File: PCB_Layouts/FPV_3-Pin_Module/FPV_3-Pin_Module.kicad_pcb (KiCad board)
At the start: 2 copper layers, 33.5 x 25.2 mm, 4 parts, among them J1 Conn_01x03_Socket, J2 Conn_01x10_Socket, J3 Conn_01x10_Socket

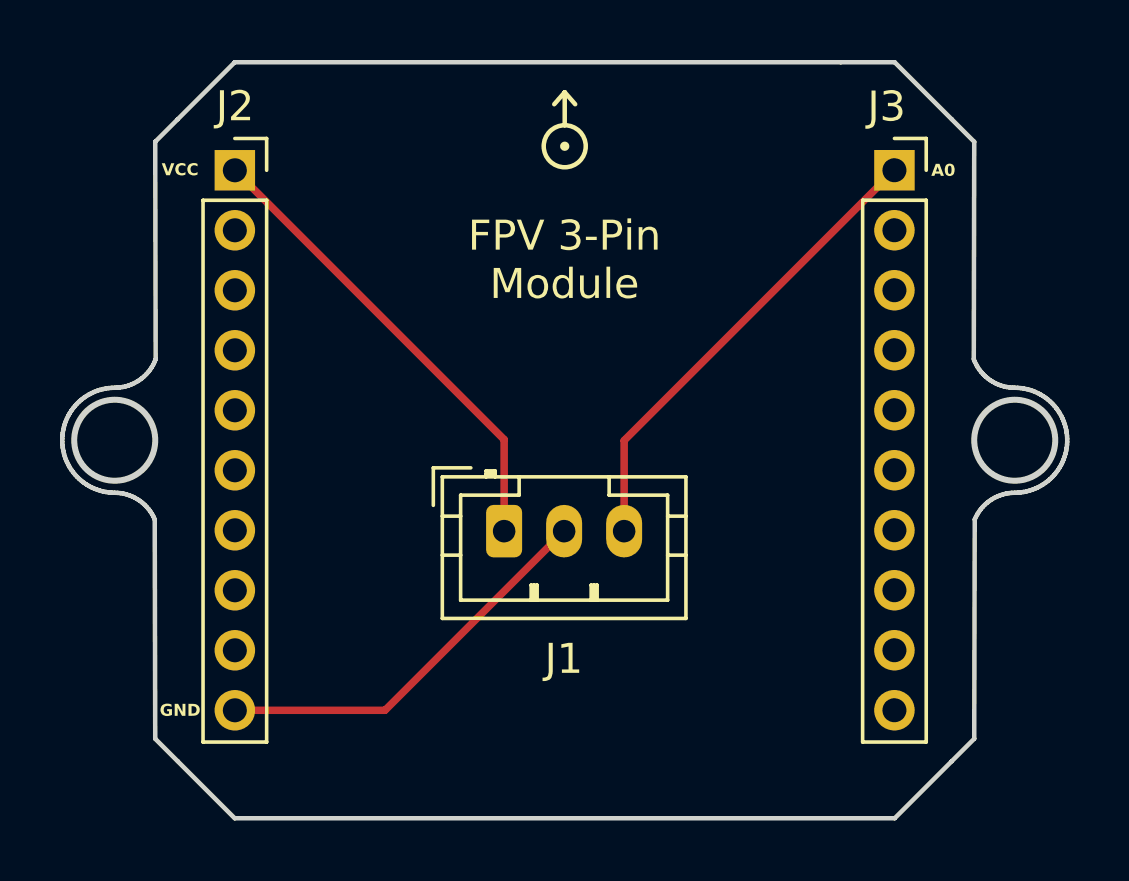
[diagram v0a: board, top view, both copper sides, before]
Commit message: Adding FPV 3 Pin quote
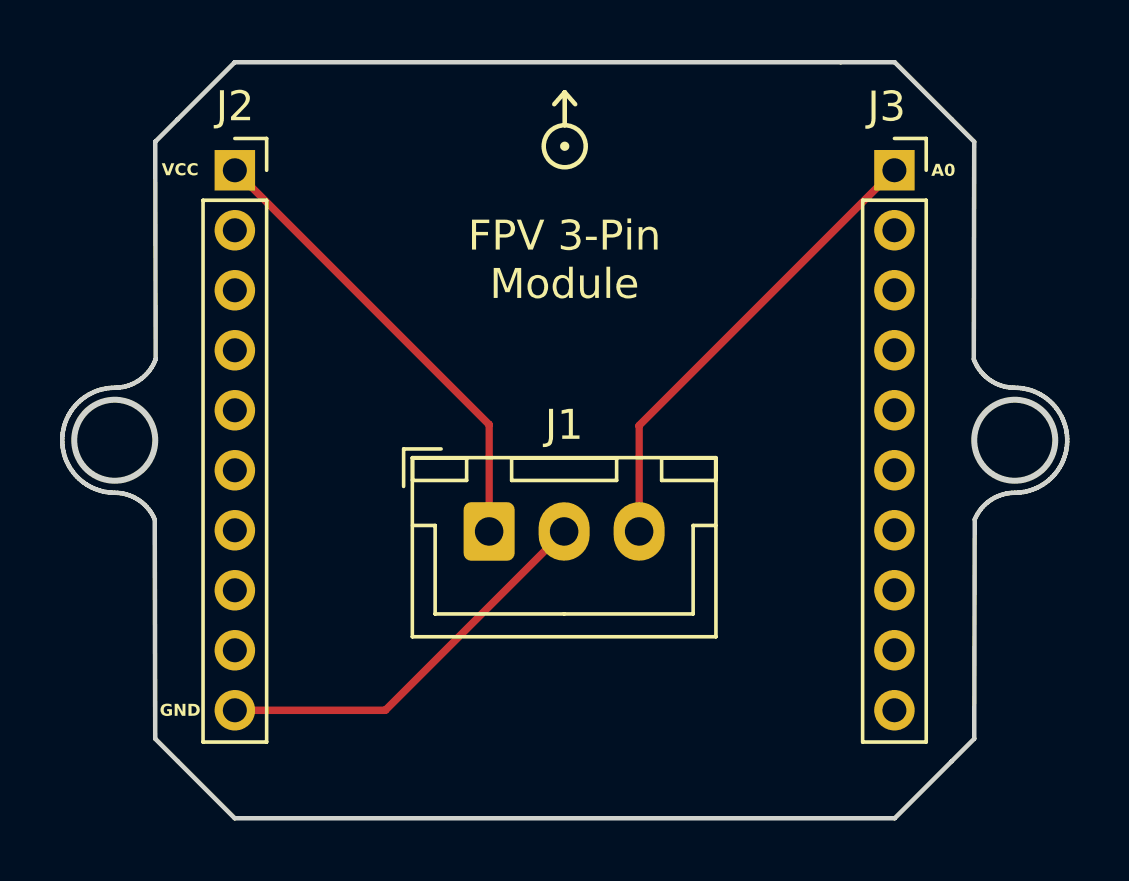
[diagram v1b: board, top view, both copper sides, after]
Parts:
- J1: footprint Connector_JST:JST_PH_B3B-PH-K_1x03_P2.00mm_Vertical -> Connector_JST:JST_XH_B3B-XH-A_1x03_P2.50mm_Vertical
- moved J1 0.50 mm to (139.1, 94.2)
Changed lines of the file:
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@@
   (net 19 "unconnected-(J3-Pin_9-Pad9)")
   (net 20 "unconnected-(J3-Pin_10-Pad10)")
-  (footprint "Connector_JST:JST_PH_B3B-PH-K_1x03_P2.00mm_Vertical" (layer "F.Cu")
-    (at 139.55 94.16)
-    (descr "JST PH series connector, B3B-PH-K (http://www.jst-mfg.com/product/pdf/eng/ePH.pdf), generated with kicad-footprint-generator")
-    (tags "connector JST PH side entry")
+  (footprint "Connector_JST:JST_XH_B3B-XH-A_1x03_P2.50mm_Vertical" (layer "F.Cu")
+    (at 139.05 94.17)
+    (descr "JST XH series connector, B3B-XH-A (http://www.jst-mfg.com/product/pdf/eng/eXH.pdf), generated with kicad-footprint-generator")
+    (tags "connector JST XH vertical")
     (property "Sheetfile" "FPV_3-Pin_Module.kicad_sch")
     (property "Sheetname" "")
@@
     (property "ki_keywords" "connector")
     (attr through_hole)
-    (fp_text reference "J1" (at 1.99 4.26) (layer "F.SilkS")
+    (fp_text reference "J1" (at 2.5 -3.55) (layer "F.SilkS")
         (effects (font (size 1 1) (thickness 0.15)))
     )
-    (fp_text value "Conn_01x03_Socket" (at 2 4) (layer "F.Fab") hide
+    (fp_text value "Conn_01x03_Socket" (at 2.5 4.6) (layer "F.Fab") hide
         (effects (font (size 1 1) (thickness 0.15)))
     )
-    (fp_text user "${REFERENCE}" (at 2 1.5) (layer "F.Fab")
+    (fp_text user "${REFERENCE}" (at 2.5 2.7) (layer "F.Fab")
         (effects (font (size 1 1) (thickness 0.15)))
     )
-    (fp_line (start -2.36 -2.11) (end -2.36 -0.86)
+    (fp_line (start -2.85 -2.75) (end -2.85 -1.5)
       (stroke (width 0.12) (type solid)) (layer "F.SilkS"))
-    (fp_line (start -2.06 -1.81) (end -2.06 2.91)
+    (fp_line (start -2.56 -2.46) (end -2.56 3.51)
       (stroke (width 0.12) (type solid)) (layer "F.SilkS"))
-    (fp_line (start -2.06 -0.5) (end -1.45 -0.5)
+    (fp_line (start -2.56 3.51) (end 7.56 3.51)
       (stroke (width 0.12) (type solid)) (layer "F.SilkS"))
-    (fp_line (start -2.06 0.8) (end -1.45 0.8)
+    (fp_line (start -2.55 -2.45) (end -2.55 -1.7)
       (stroke (width 0.12) (type solid)) (layer "F.SilkS"))
-    (fp_line (start -2.06 2.91) (end 6.06 2.91)
+    (fp_line (start -2.55 -1.7) (end -0.75 -1.7)
       (stroke (width 0.12) (type solid)) (layer "F.SilkS"))
-    (fp_line (start -1.45 -1.2) (end -1.45 2.3)
+    (fp_line (start -2.55 -0.2) (end -1.8 -0.2)
       (stroke (width 0.12) (type solid)) (layer "F.SilkS"))
-    (fp_line (start -1.45 2.3) (end 5.45 2.3)
+    (fp_line (start -1.8 -0.2) (end -1.8 2.75)
       (stroke (width 0.12) (type solid)) (layer "F.SilkS"))
-    (fp_line (start -1.11 -2.11) (end -2.36 -2.11)
+    (fp_line (start -1.8 2.75) (end 2.5 2.75)
       (stroke (width 0.12) (type solid)) (layer "F.SilkS"))
-    (fp_line (start -0.6 -2.01) (end -0.6 -1.81)
+    (fp_line (start -1.6 -2.75) (end -2.85 -2.75)
       (stroke (width 0.12) (type solid)) (layer "F.SilkS"))
-    (fp_line (start -0.3 -2.01) (end -0.6 -2.01)
+    (fp_line (start -0.75 -2.45) (end -2.55 -2.45)
       (stroke (width 0.12) (type solid)) (layer "F.SilkS"))
-    (fp_line (start -0.3 -1.91) (end -0.6 -1.91)
+    (fp_line (start -0.75 -1.7) (end -0.75 -2.45)
       (stroke (width 0.12) (type solid)) (layer "F.SilkS"))
-    (fp_line (start -0.3 -1.81) (end -0.3 -2.01)
+    (fp_line (start 0.75 -2.45) (end 0.75 -1.7)
       (stroke (width 0.12) (type solid)) (layer "F.SilkS"))
-    (fp_line (start 0.5 -1.81) (end 0.5 -1.2)
+    (fp_line (start 0.75 -1.7) (end 4.25 -1.7)
       (stroke (width 0.12) (type solid)) (layer "F.SilkS"))
-    (fp_line (start 0.5 -1.2) (end -1.45 -1.2)
+    (fp_line (start 4.25 -2.45) (end 0.75 -2.45)
       (stroke (width 0.12) (type solid)) (layer "F.SilkS"))
-    (fp_line (start 0.9 1.8) (end 1.1 1.8)
+    (fp_line (start 4.25 -1.7) (end 4.25 -2.45)
       (stroke (width 0.12) (type solid)) (layer "F.SilkS"))
-    (fp_line (start 0.9 2.3) (end 0.9 1.8)
+    (fp_line (start 5.75 -2.45) (end 5.75 -1.7)
       (stroke (width 0.12) (type solid)) (layer "F.SilkS"))
-    (fp_line (start 1 2.3) (end 1 1.8)
+    (fp_line (start 5.75 -1.7) (end 7.55 -1.7)
       (stroke (width 0.12) (type solid)) (layer "F.SilkS"))
-    (fp_line (start 1.1 1.8) (end 1.1 2.3)
+    (fp_line (start 6.8 -0.2) (end 6.8 2.75)
       (stroke (width 0.12) (type solid)) (layer "F.SilkS"))
-    (fp_line (start 2.9 1.8) (end 3.1 1.8)
+    (fp_line (start 6.8 2.75) (end 2.5 2.75)
       (stroke (width 0.12) (type solid)) (layer "F.SilkS"))
-    (fp_line (start 2.9 2.3) (end 2.9 1.8)
+    (fp_line (start 7.55 -2.45) (end 5.75 -2.45)
       (stroke (width 0.12) (type solid)) (layer "F.SilkS"))
-    (fp_line (start 3 2.3) (end 3 1.8)
+    (fp_line (start 7.55 -1.7) (end 7.55 -2.45)
       (stroke (width 0.12) (type solid)) (layer "F.SilkS"))
-    (fp_line (start 3.1 1.8) (end 3.1 2.3)
+    (fp_line (start 7.55 -0.2) (end 6.8 -0.2)
       (stroke (width 0.12) (type solid)) (layer "F.SilkS"))
-    (fp_line (start 3.5 -1.2) (end 3.5 -1.81)
+    (fp_line (start 7.56 -2.46) (end -2.56 -2.46)
       (stroke (width 0.12) (type solid)) (layer "F.SilkS"))
-    (fp_line (start 5.45 -1.2) (end 3.5 -1.2)
+    (fp_line (start 7.56 3.51) (end 7.56 -2.46)
       (stroke (width 0.12) (type solid)) (layer "F.SilkS"))
-    (fp_line (start 5.45 2.3) (end 5.45 -1.2)
-      (stroke (width 0.12) (type solid)) (layer "F.SilkS"))
-    (fp_line (start 6.06 -1.81) (end -2.06 -1.81)
-      (stroke (width 0.12) (type solid)) (layer "F.SilkS"))
-    (fp_line (start 6.06 -0.5) (end 5.45 -0.5)
-      (stroke (width 0.12) (type solid)) (layer "F.SilkS"))
-    (fp_line (start 6.06 0.8) (end 5.45 0.8)
-      (stroke (width 0.12) (type solid)) (layer "F.SilkS"))
-    (fp_line (start 6.06 2.91) (end 6.06 -1.81)
-      (stroke (width 0.12) (type solid)) (layer "F.SilkS"))
-    (fp_line (start -2.45 -2.2) (end -2.45 3.3)
+    (fp_line (start -2.95 -2.85) (end -2.95 3.9)
       (stroke (width 0.05) (type solid)) (layer "F.CrtYd"))
-    (fp_line (start -2.45 3.3) (end 6.45 3.3)
+    (fp_line (start -2.95 3.9) (end 7.95 3.9)
       (stroke (width 0.05) (type solid)) (layer "F.CrtYd"))
-    (fp_line (start 6.45 -2.2) (end -2.45 -2.2)
+    (fp_line (start 7.95 -2.85) (end -2.95 -2.85)
       (stroke (width 0.05) (type solid)) (layer "F.CrtYd"))
-    (fp_line (start 6.45 3.3) (end 6.45 -2.2)
+    (fp_line (start 7.95 3.9) (end 7.95 -2.85)
       (stroke (width 0.05) (type solid)) (layer "F.CrtYd"))
-    (fp_line (start -2.36 -2.11) (end -2.36 -0.86)
+    (fp_line (start -2.45 -2.35) (end -2.45 3.4)
       (stroke (width 0.1) (type solid)) (layer "F.Fab"))
-    (fp_line (start -1.95 -1.7) (end -1.95 2.8)
+    (fp_line (start -2.45 3.4) (end 7.45 3.4)
       (stroke (width 0.1) (type solid)) (layer "F.Fab"))
-    (fp_line (start -1.95 2.8) (end 5.95 2.8)
+    (fp_line (start -0.625 -2.35) (end 0 -1.35)
       (stroke (width 0.1) (type solid)) (layer "F.Fab"))
-    (fp_line (start -1.11 -2.11) (end -2.36 -2.11)
+    (fp_line (start 0 -1.35) (end 0.625 -2.35)
       (stroke (width 0.1) (type solid)) (layer "F.Fab"))
-    (fp_line (start 5.95 -1.7) (end -1.95 -1.7)
+    (fp_line (start 7.45 -2.35) (end -2.45 -2.35)
       (stroke (width 0.1) (type solid)) (layer "F.Fab"))
-    (fp_line (start 5.95 2.8) (end 5.95 -1.7)
+    (fp_line (start 7.45 3.4) (end 7.45 -2.35)
       (stroke (width 0.1) (type solid)) (layer "F.Fab"))
-    (pad "1" thru_hole roundrect (at 0 0) (size 1.2 1.75) (drill 0.75) (layers "*.Cu" "*.Mask") (roundrect_rratio 0.2083333333)
+    (pad "1" thru_hole roundrect (at 0 0) (size 1.7 1.95) (drill 0.95) (layers "*.Cu" "*.Mask") (roundrect_rratio 0.147059)
       (net 1 "Net-(J1-Pin_1)") (pinfunction "Pin_1") (pintype "passive"))
-    (pad "2" thru_hole oval (at 2 0) (size 1.2 1.75) (drill 0.75) (layers "*.Cu" "*.Mask")
+    (pad "2" thru_hole oval (at 2.5 0) (size 1.7 1.95) (drill 0.95) (layers "*.Cu" "*.Mask")
       (net 2 "Net-(J1-Pin_2)") (pinfunction "Pin_2") (pintype "passive"))
-    (pad "3" thru_hole oval (at 4 0) (size 1.2 1.75) (drill 0.75) (layers "*.Cu" "*.Mask")
+    (pad "3" thru_hole oval (at 5 0) (size 1.7 1.95) (drill 0.95) (layers "*.Cu" "*.Mask")
       (net 3 "Net-(J1-Pin_3)") (pinfunction "Pin_3") (pintype "passive"))
-    (model "${KICAD6_3DMODEL_DIR}/Connector_JST.3dshapes/JST_PH_B3B-PH-K_1x03_P2.00mm_Vertical.wrl"
+    (model "${KICAD6_3DMODEL_DIR}/Connector_JST.3dshapes/JST_XH_B3B-XH-A_1x03_P2.50mm_Vertical.wrl"
       (offset (xyz 0 0 0))
       (scale (xyz 1 1 1))
@@
     (effects (font (size 1 1) (thickness 0.25)))
   )
-  (segment (start 139.55 91.1072) (end 130.5738 82.131) (width 0.25) (layer "F.Cu") (net 1))
-  (segment (start 139.55 94.16) (end 139.55 91.1072) (width 0.25) (layer "F.Cu") (net 1))
-  (segment (start 141.55 94.16) (end 135.579 100.131) (width 0.25) (layer "F.Cu") (net 2))
-  (segment (start 135.579 100.131) (end 130.5738 100.131) (width 0.25) (layer "F.Cu") (net 2))
-  (segment (start 143.55 94.16) (end 143.55 91.14) (width 0.25) (layer "F.Cu") (net 3))
-  (segment (start 143.55 91.14) (end 152.56 82.13) (width 0.25) (layer "F.Cu") (net 3))
+  (segment (start 139.05 94.17) (end 139.05 90.6072) (width 0.25) (layer "F.Cu") (net 1))
+  (segment (start 139.05 90.6072) (end 130.5738 82.131) (width 0.25) (layer "F.Cu") (net 1))
+  (segment (start 135.589 100.131) (end 130.5738 100.131) (width 0.25) (layer "F.Cu") (net 2))
+  (segment (start 141.55 94.17) (end 135.589 100.131) (width 0.25) (layer "F.Cu") (net 2))
+  (segment (start 144.05 90.64) (end 152.56 82.13) (width 0.25) (layer "F.Cu") (net 3))
+  (segment (start 144.05 94.17) (end 144.05 90.64) (width 0.25) (layer "F.Cu") (net 3))
 )

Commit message: Adding FPV 4 Pin quote
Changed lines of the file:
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@@
     (fp_line (start 7.45 3.4) (end 7.45 -2.35)
       (stroke (width 0.1) (type solid)) (layer "F.Fab"))
-    (pad "1" thru_hole roundrect (at 0 0) (size 1.7 1.95) (drill 0.95) (layers "*.Cu" "*.Mask") (roundrect_rratio 0.147059)
+    (pad "1" thru_hole roundrect (at 0 0) (size 1.7 1.95) (drill 0.95) (layers "*.Cu" "*.Mask") (roundrect_rratio 0.1470588235)
       (net 1 "Net-(J1-Pin_1)") (pinfunction "Pin_1") (pintype "passive"))
     (pad "2" thru_hole oval (at 2.5 0) (size 1.7 1.95) (drill 0.95) (layers "*.Cu" "*.Mask")
